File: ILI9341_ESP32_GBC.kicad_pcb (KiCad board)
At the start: 2 copper layers, 70 x 122.2 mm, 124 parts, among them CN1 KH-CL0.5-H2.0-18PS, J1 USB_C_Receptacle_USB2.0_16P, J2 Conn_01x05_Pin, J5 Micro_SD_Card_CD, J6 Conn_01x18_Socket, Q10 XYC-PT204B-L1, Q2 BC817, SW1 TM-2023, SW10 SW_Push, SW11 SW_Push, SW12 SW_Push, SW2 SW_Push, SW3 SW_Push, SW4 SW_Push, SW5 SW_Push, SW6 K3-1290S-J1, SW7 SW_Push, SW8 SW_Push, SW9 SW_Push, U2 XM5062S, U3 LM358LVIDDFR, U4 BQ25171QWDRCRQ1, U7 ESP32-S3-WROOM-1-N16R8, U8 MAX98357AETE+T, U9 TPS61028DRCR

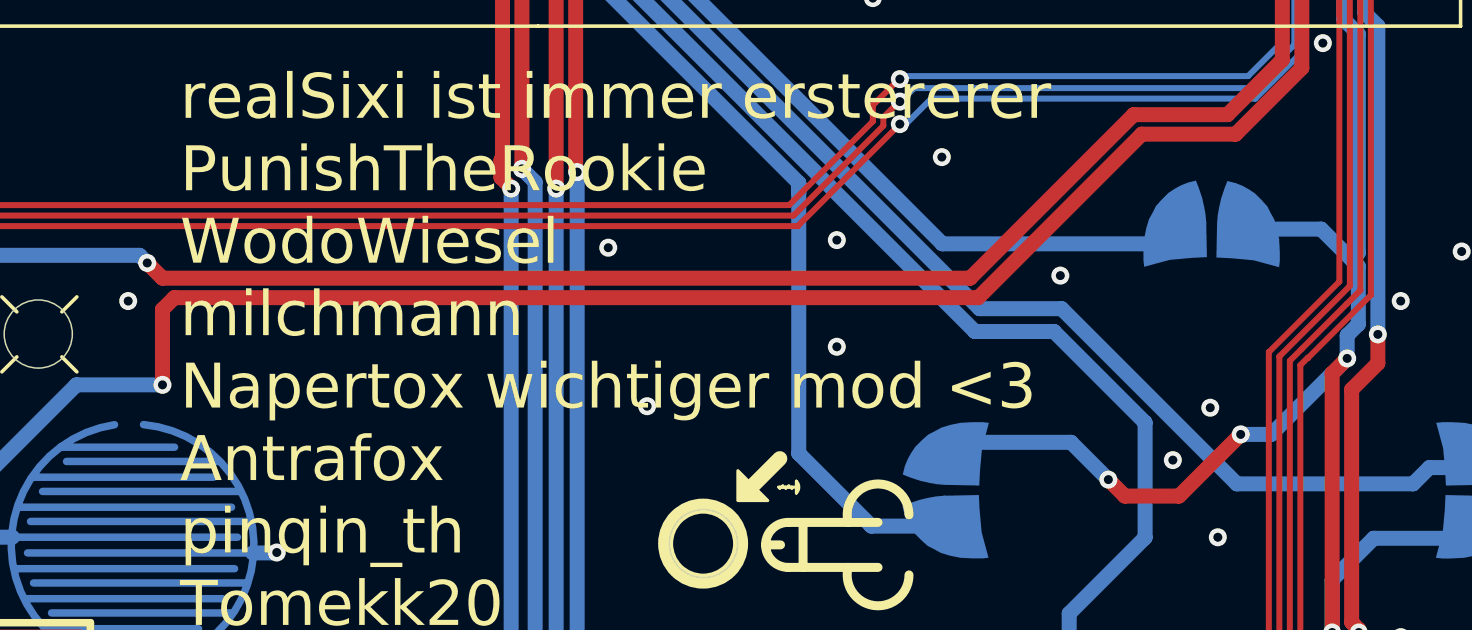
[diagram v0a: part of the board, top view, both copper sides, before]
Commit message: update carstenbl7 in silkscreen
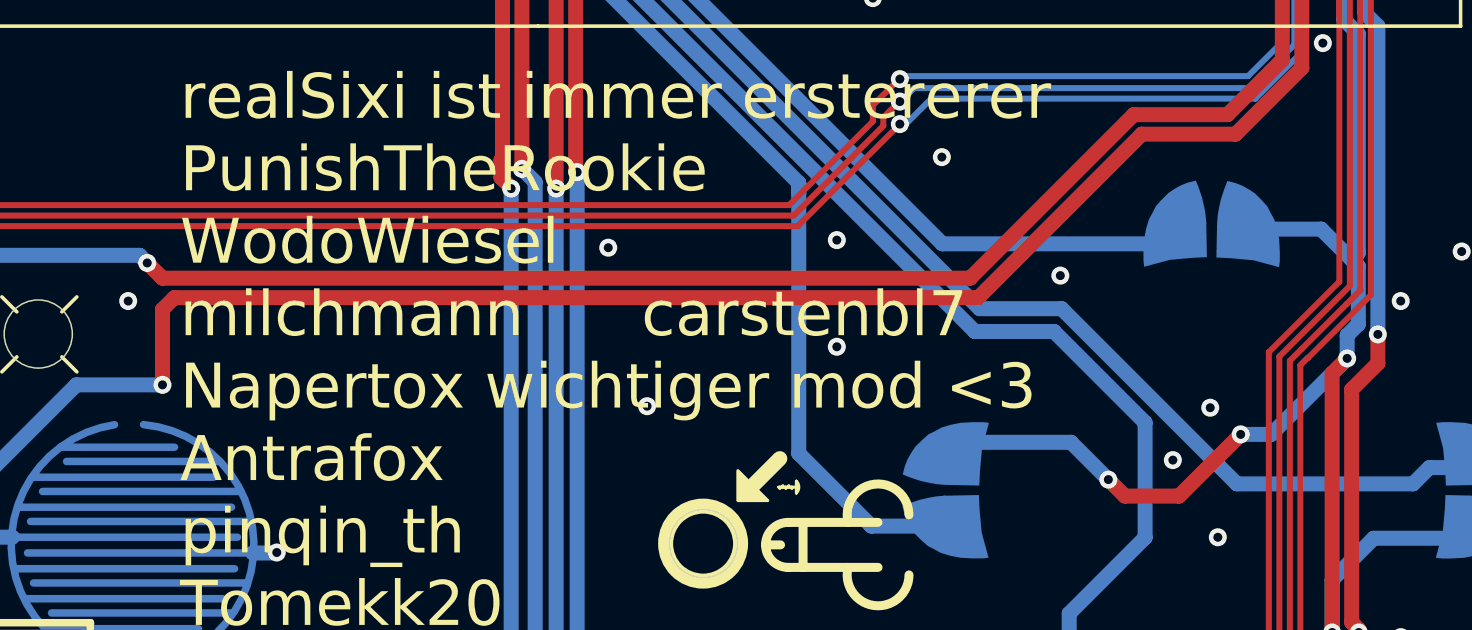
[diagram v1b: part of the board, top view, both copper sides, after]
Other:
- board text added: "realSixi ist immer erstererer PunishTheRookie WodoWiesel milchmann carstenbl7 Napertox wichtiger mod <3 Antrafox pinqin_th Tomekk20 noch_online lieblings mod :* der_Digga meins_da Naegolus HeroAAX yeTTizTV rsger12 Schattenwelt Opel_Calibra_16V Schnullerin Schnuller"
- board text removed: "realSixi ist immer erstererer PunishTheRookie WodoWiesel milchmann Napertox wichtiger mod <3 Antrafox pinqin_th Tomekk20 noch_online lieblings mod :* der_Digga meins_da Naegolus HeroAAX yeTTizTV rsger12 Schattenwelt Opel_Calibra_16V Schnullerin Schnuller"
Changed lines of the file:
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@@
 		(tags "LED")
 		(property "Reference" "D5"
-			(at 0 1.43 360)
+			(at 0 1.43 0)
 			(layer "B.SilkS")
 			(effects
@@
 		)
 		(property "Value" "LED"
-			(at 0 -1.43 360)
+			(at 0 -1.43 0)
 			(layer "B.Fab")
 			(effects
@@
 		)
 		(fp_text user "${REFERENCE}"
-			(at 0 0 360)
+			(at 0 0 0)
 			(layer "B.Fab")
 			(effects
@@
 		)
 	)
-	(gr_text "realSixi ist immer erstererer\nPunishTheRookie\nWodoWiesel\nmilchmann\nNapertox wichtiger mod <3\nAntrafox\npinqin_th\nTomekk20\nnoch_online lieblings mod :*\nder_Digga\nmeins_da\nNaegolus\nHeroAAX    yeTTizTV\nrsger12    Schattenwelt\nOpel_Calibra_16V\nSchnullerin\nSchnuller\n"
+	(gr_text "realSixi ist immer erstererer\nPunishTheRookie\nWodoWiesel\nmilchmann      carstenbl7\nNapertox wichtiger mod <3\nAntrafox\npinqin_th\nTomekk20\nnoch_online lieblings mod :*\nder_Digga\nmeins_da\nNaegolus\nHeroAAX    yeTTizTV\nrsger12    Schattenwelt\nOpel_Calibra_16V\nSchnullerin\nSchnuller\n"
 		(at 130.5052 143.7132 0)
 		(layer "F.SilkS")

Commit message: Upload order version 1.3
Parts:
- removed D7: ZIR034, TheBrutzlers_Lib:SIDE_LED_IR_3mm
- removed Q10: XYC-PT204B-L1, TheBrutzlers_Lib:SIDE_LED_IR_3mm
- removed SW6: K3-1290S-J1, easyeda2kicad:SW-SMD_K3-1290S-J1
- added SW13: MSK12CO2-SZ, easyeda2kicad:SW-TH_MSK12C02, F.Cu at (113.5, 65.2)
- added U1: VSMB10940, easyeda2kicad:LED-SMD_3P-L3.0-W1.0-FD, F.Cu at (162.3, 39.2)
- added U5: PT12-21B/TR8, easyeda2kicad:LED-SMD_3P-L3.0-W1.0-FD, F.Cu at (168.4, 39.2)
- L3: value 2.2µ -> 10µ
- moved BT2 2.00 mm to (121.3, 126.5)
- moved FPC1 0.80 mm to (153.4, 62.0)
- moved J6 0.80 mm to (153.4, 62.0)
- moved BT1 0.50 mm to (112.0, 111.0)
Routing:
- net +3V3: track 396.1 -> 405.0 mm
- net Net-(R47-Pad1): track 2.61 -> 8.64 mm
- net Net-(R14-Pad2): track 4.23 -> 8.51 mm
- net /LCD_CLK: track 33.7 -> 32.6 mm
- net /I2C_CLK: track 39.5 -> 38.7 mm
- net /BAT+: track 54.6 -> 53.9 mm
- net /VUSB: track 166.6 -> 166.1 mm
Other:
- outline, holes or cut-outs redrawn
- board text added: "1.3"
- board text removed: "1.2"
